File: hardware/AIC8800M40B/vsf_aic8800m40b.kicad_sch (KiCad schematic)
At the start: 102 parts, among them J1 USB_A, J2 USB_C_Receptacle_USB2.0, J3 USB_C_Receptacle_USB2.0, J4 Micro_SD_Card_Det1, J6 Conn_Coaxial, J7 Conn_Coaxial, J8 Conn_01x05, Q1 S9013, SW1 SW_Push, SW2 SW_Push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

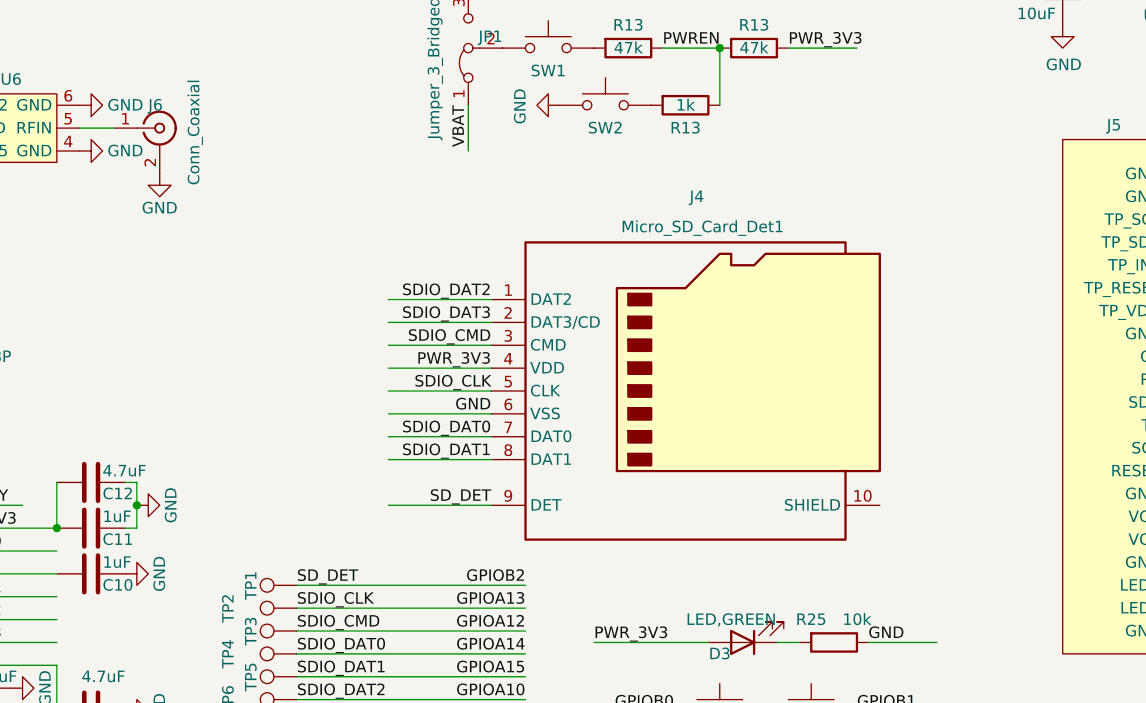
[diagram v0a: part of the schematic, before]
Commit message: [hardware/aic8800m40b] update to add 2.54 ext port
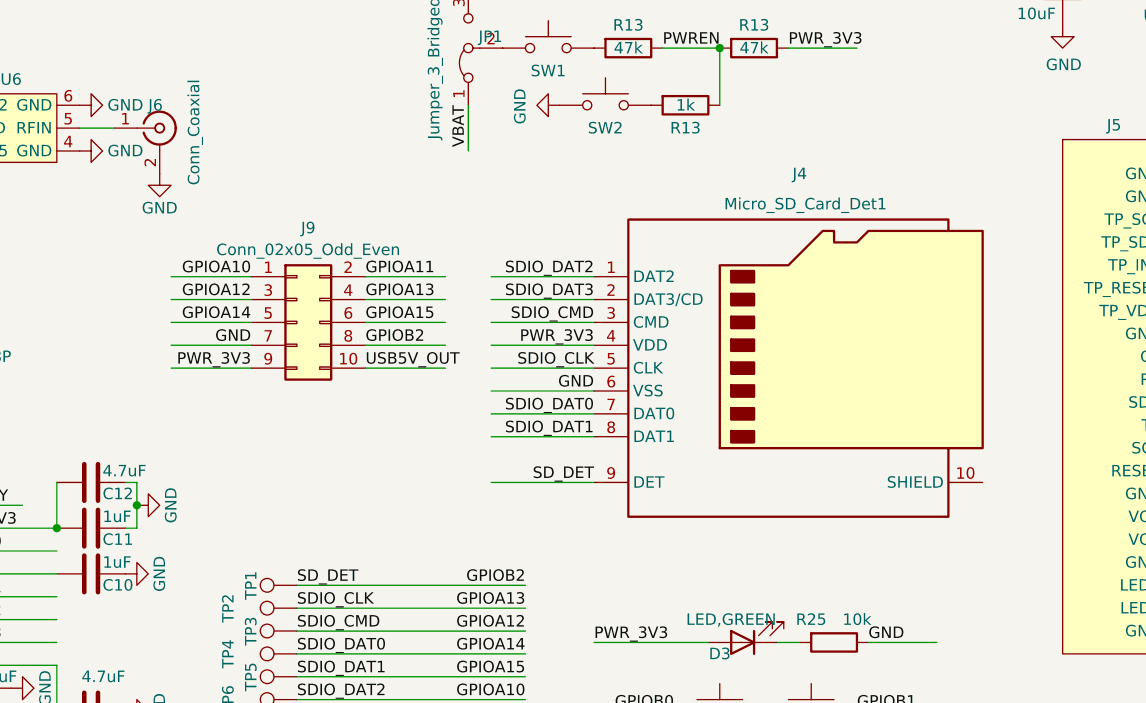
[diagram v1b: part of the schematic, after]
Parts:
- added J9: Conn_02x05_Odd_Even, Connector_PinHeader_2.54mm:PinHeader_2x05_P2.54mm_Horizontal, symbol Connector_Generic:Conn_02x05_Odd_Even
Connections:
- net GND: now also J9.7 (Pin_7)
- net GPIOA10: now also J9.1 (Pin_1)
- net GPIOA11: now also J9.2 (Pin_2)
- net GPIOA12: now also J9.3 (Pin_3)
- net GPIOA13: now also J9.4 (Pin_4)
- net GPIOA14: now also J9.5 (Pin_5)
- net GPIOA15: now also J9.6 (Pin_6)
- net GPIOB2: now also J9.8 (Pin_8)
- net PWR_3V3: now also J9.9 (Pin_9)
- net USB5V_OUT: now also J9.10 (Pin_10)
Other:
- moved on the sheet: J4

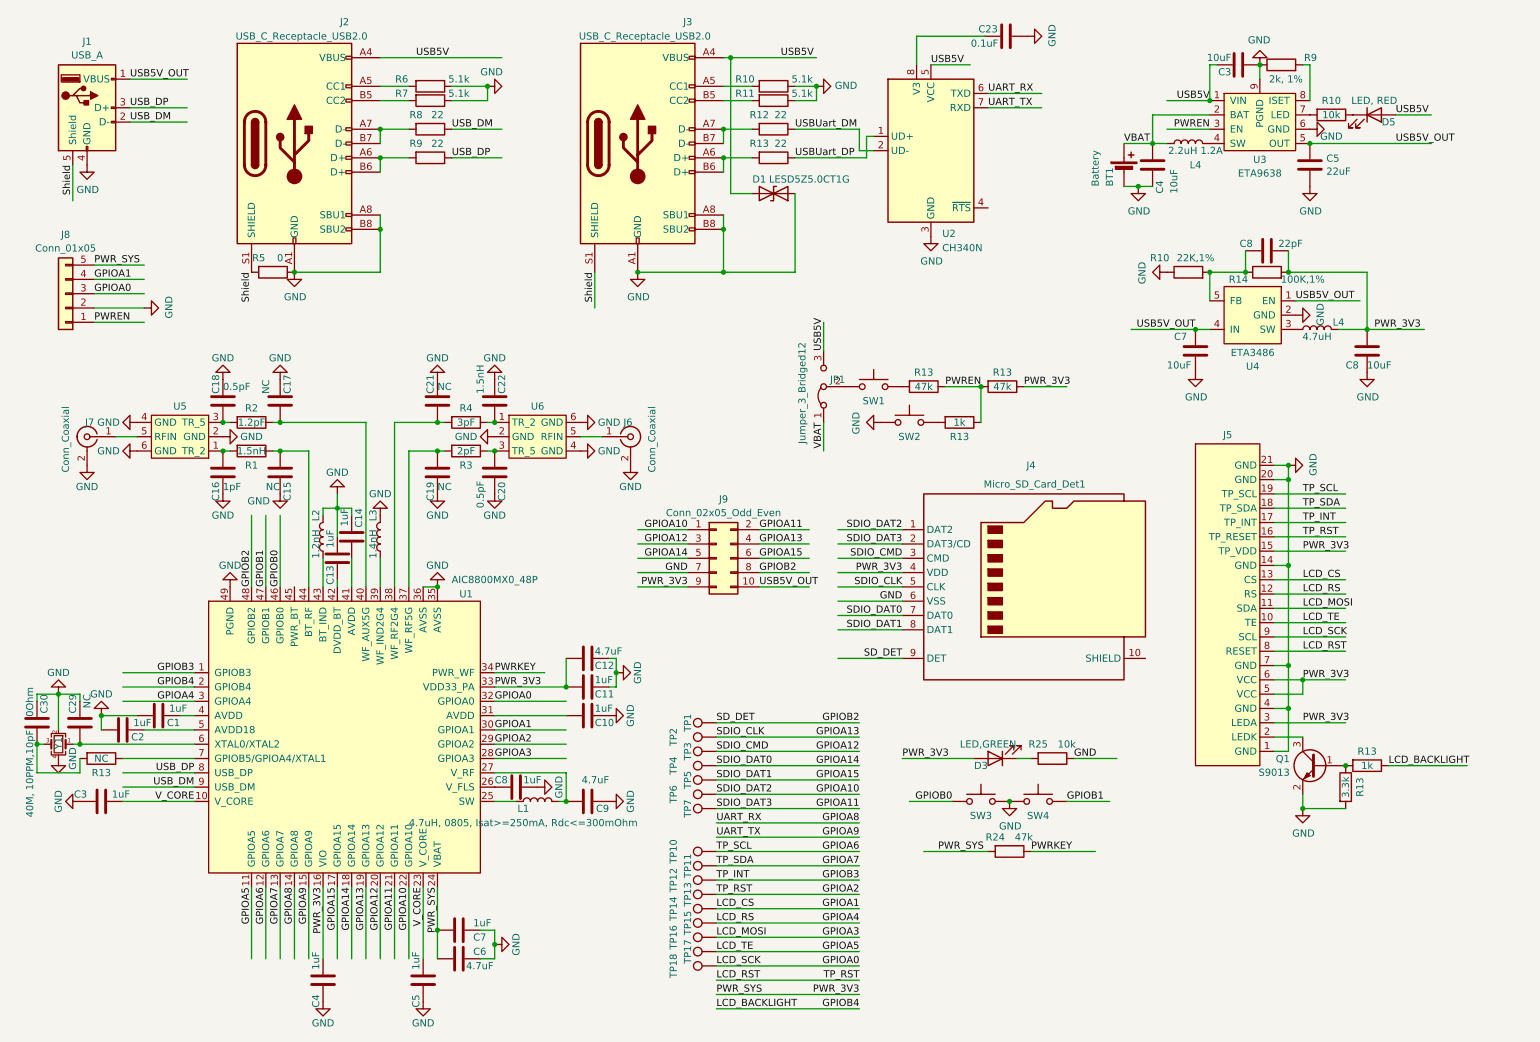
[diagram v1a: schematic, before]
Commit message: [hardware/aic8800m40b] add connector for all GPIOs
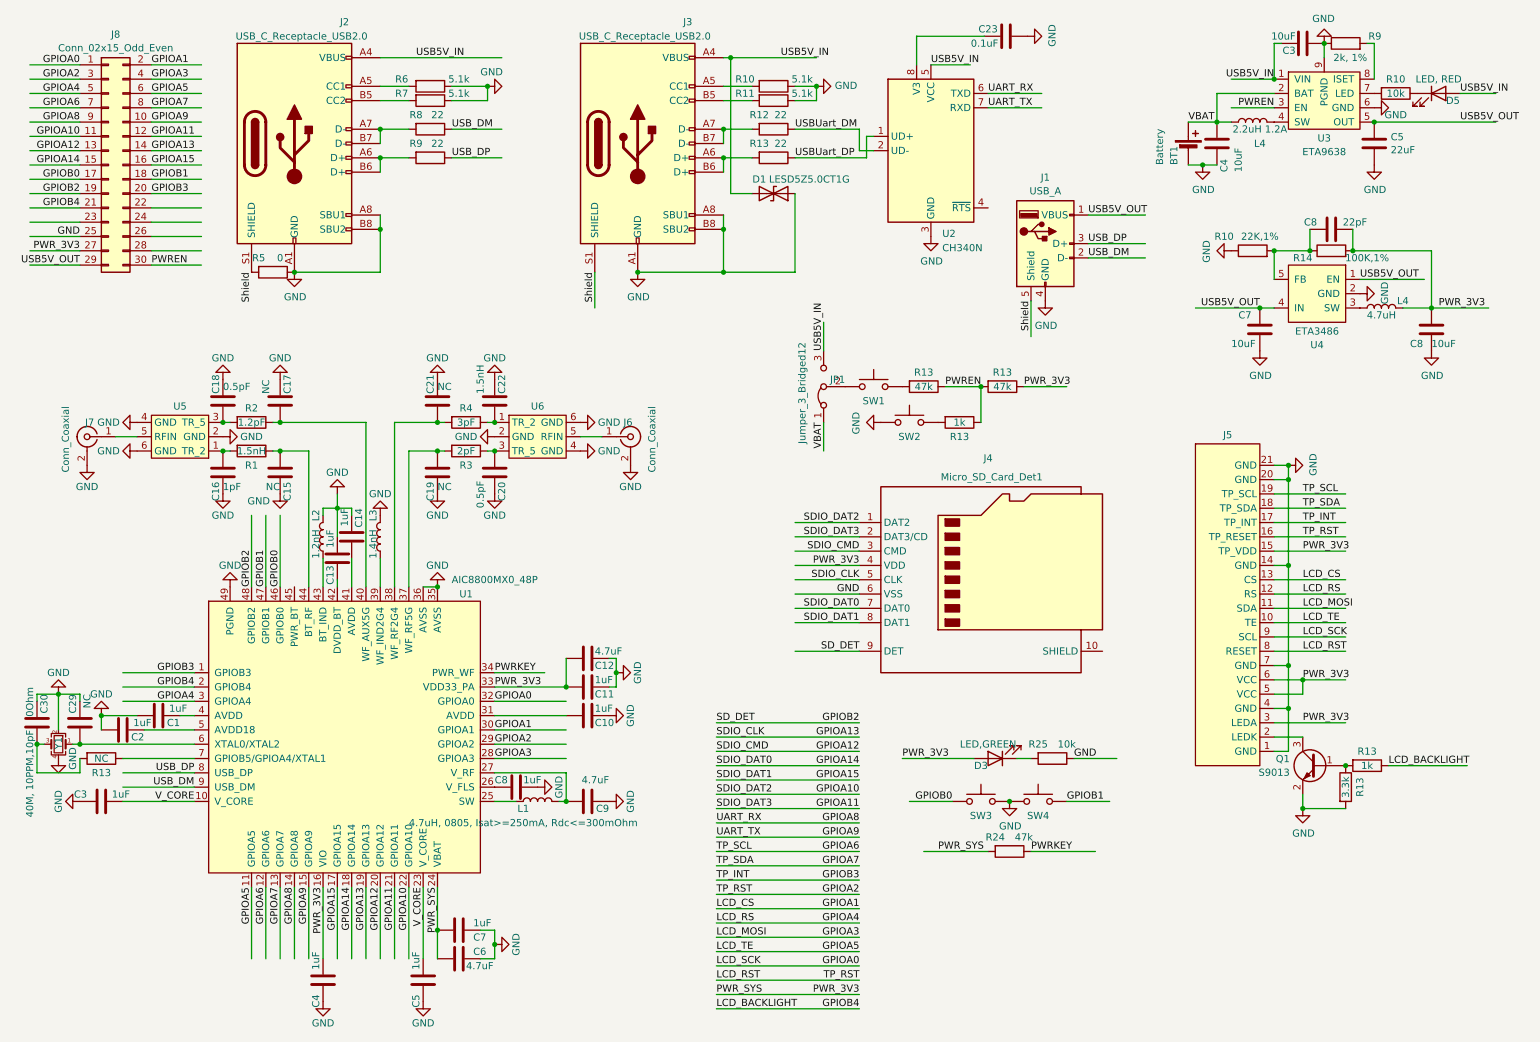
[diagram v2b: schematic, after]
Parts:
- removed J8: Conn_01x05, Connector_Harwin:Harwin_M20-89005xx_1x05_P2.54mm_Horizontal, symbol Connector_Generic:Conn_01x05
- removed J9: Conn_02x05_Odd_Even, Connector_PinHeader_2.54mm:PinHeader_2x05_P2.54mm_Horizontal, symbol Connector_Generic:Conn_02x05_Odd_Even
- removed TP1, TP10, TP11, TP12, TP13, TP14, TP15, TP16, TP17, TP18, TP2, TP3, TP4, TP5, TP6, TP7: TestPoint, TestPoint:TestPoint_Pad_D1.0mm, symbol Connector:TestPoint
- added J8: Conn_02x15_Odd_Even, Connector_PinHeader_2.54mm:PinHeader_2x15_P2.54mm_Horizontal, symbol Connector_Generic:Conn_02x15_Odd_Even
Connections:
- net GND: now also J8.25 (Pin_25)
- net GPIOA0: now also J8.1 (Pin_1)
- net GPIOA1: now also J8.2 (Pin_2)
- net GPIOA10: now also J8.11 (Pin_11)
- net GPIOA11: now also J8.12 (Pin_12)
- net GPIOA12: now also J8.13 (Pin_13)
- net GPIOA13: now also J8.14 (Pin_14)
- net GPIOA14: now also J8.15 (Pin_15)
- net GPIOA15: now also J8.16 (Pin_16)
- net GPIOA2: now also J8.3 (Pin_3)
- net GPIOA3: now also J8.4 (Pin_4)
- net GPIOA4: now also J8.5 (Pin_5)
- net GPIOA5: now also J8.6 (Pin_6)
- net GPIOA6: now also J8.7 (Pin_7)
- net GPIOA7: now also J8.8 (Pin_8)
- net GPIOA8: now also J8.9 (Pin_9)
- net GPIOA9: now also J8.10 (Pin_10)
- net GPIOB0: now also J8.17 (Pin_17)
- net GPIOB1: now also J8.18 (Pin_18)
- net GPIOB2: now also J8.19 (Pin_19)
- net GPIOB3: now also J8.20 (Pin_20)
- net GPIOB4: now also J8.21 (Pin_21)
- net PWREN: now also J8.30 (Pin_30)
- net PWR_3V3: now also J8.27 (Pin_27)
- net USB5V_OUT: now also J8.29 (Pin_29)
- net USB5V renamed USB5V_IN
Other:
- moved on the sheet: BT1, C3, C4, C5, C7, C8, D5, J1, J4, L4, R10, R14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

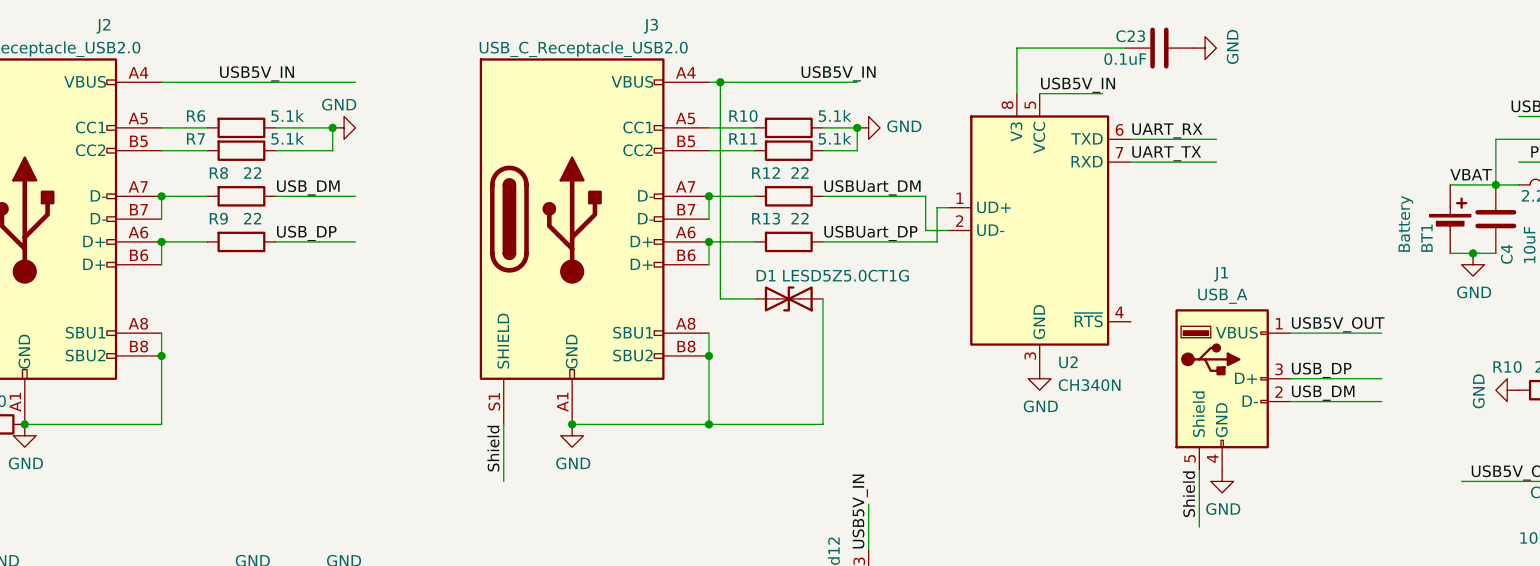
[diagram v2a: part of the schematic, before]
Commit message: [hardware/aic8800m40b] fix USB-A signals
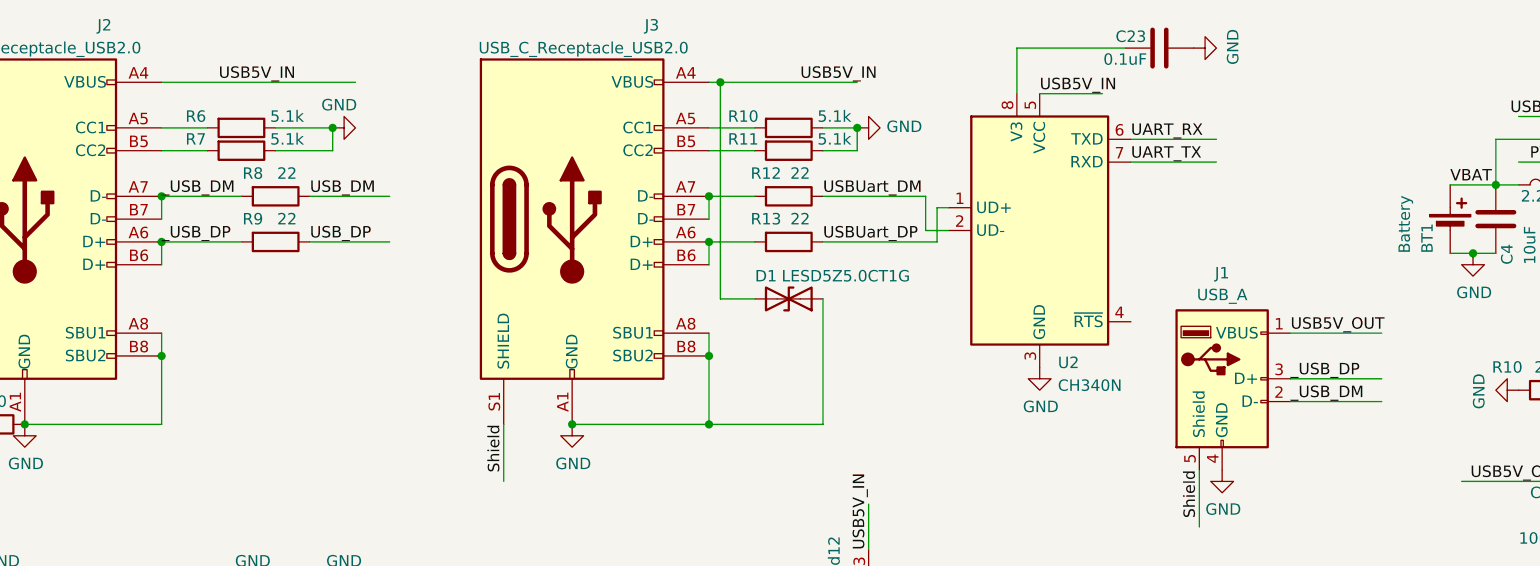
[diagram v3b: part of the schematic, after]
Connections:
- net USB_DM: no longer J1.2 (D-)
- net USB_DP: no longer J1.3 (D+)
- net _USB_DP: now reaches J2.A6 (D+), J2.B6 (D+), R9.2
- net _USB_DP: now also J1.3 (D+)
- net _USB_DM: now reaches J2.A7 (D-), J2.B7 (D-), R8.2
- net _USB_DM: now also J1.2 (D-)
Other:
- moved on the sheet: R8, R9
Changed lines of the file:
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@@
     (stroke (width 0) (type default))
   )
-  (wire (pts (xy 80.01 39.37) (xy 85.09 39.37))
+  (wire (pts (xy 80.01 39.37) (xy 88.9 39.37))
     (stroke (width 0) (type default))
   )
@@
     (stroke (width 0) (type default))
   )
-  (wire (pts (xy 92.71 34.29) (xy 101.6 34.29))
+  (wire (pts (xy 96.52 34.29) (xy 105.41 34.29))
     (stroke (width 0) (type default))
   )
@@
     (stroke (width 0) (type default))
   )
-  (wire (pts (xy 80.01 34.29) (xy 85.09 34.29))
+  (wire (pts (xy 80.01 34.29) (xy 88.9 34.29))
     (stroke (width 0) (type default))
   )
@@
     (stroke (width 0) (type default))
   )
-  (wire (pts (xy 92.71 39.37) (xy 101.6 39.37))
+  (wire (pts (xy 96.52 39.37) (xy 105.41 39.37))
     (stroke (width 0) (type default))
   )
@@
     (effects (font (size 1.27 1.27)) (justify right bottom))
   )
-  (label "USB_DP" (at 92.71 39.37 0) (fields_autoplaced)
+  (label "USB_DP" (at 96.52 39.37 0) (fields_autoplaced)
     (effects (font (size 1.27 1.27)) (justify left bottom))
   )
-  (label "USB_DP" (at 205.74 54.61 0) (fields_autoplaced)
+  (label "_USB_DP" (at 205.74 54.61 0) (fields_autoplaced)
     (effects (font (size 1.27 1.27)) (justify left bottom))
   )
@@
     (effects (font (size 1.27 1.27)) (justify right bottom))
   )
+  (label "_USB_DP" (at 80.01 39.37 0) (fields_autoplaced)
+    (effects (font (size 1.27 1.27)) (justify left bottom))
+  )
   (label "PWR_SYS" (at 139.7 187.96 0) (fields_autoplaced)
     (effects (font (size 1.27 1.27)) (justify left bottom))
@@
     (effects (font (size 1.27 1.27)) (justify right bottom))
   )
+  (label "_USB_DM" (at 80.01 34.29 0) (fields_autoplaced)
+    (effects (font (size 1.27 1.27)) (justify left bottom))
+  )
   (label "GPIOA6" (at 26.67 30.48 180) (fields_autoplaced)
     (effects (font (size 1.27 1.27)) (justify right bottom))
@@
     (effects (font (size 1.27 1.27)) (justify right bottom))
   )
-  (label "USB_DM" (at 205.74 57.15 0) (fields_autoplaced)
+  (label "_USB_DM" (at 205.74 57.15 0) (fields_autoplaced)
     (effects (font (size 1.27 1.27)) (justify left bottom))
   )
@@
     (effects (font (size 1.27 1.27)) (justify left bottom))
   )
-  (label "USB_DM" (at 92.71 34.29 0) (fields_autoplaced)
+  (label "USB_DM" (at 96.52 34.29 0) (fields_autoplaced)
     (effects (font (size 1.27 1.27)) (justify left bottom))
   )
@@
     )
   )
-  (symbol (lib_id "Device:R") (at 88.9 34.29 270) (unit 1)
+  (symbol (lib_id "Device:R") (at 92.71 34.29 270) (unit 1)
     (in_bom yes) (on_board yes) (dnp no)
-    (property "Reference" "R8" (at 86.36 31.75 90)
+    (property "Reference" "R8" (at 90.17 31.75 90)
       (effects (font (size 1.27 1.27)))
     )
-    (property "Value" "22" (at 90.17 31.75 90)
+    (property "Value" "22" (at 93.98 31.75 90)
       (effects (font (size 1.27 1.27)))
     )
-    (property "Footprint" "Resistor_SMD:R_0402_1005Metric" (at 88.9 32.512 90)
+    (property "Footprint" "Resistor_SMD:R_0402_1005Metric" (at 92.71 32.512 90)
       (effects (font (size 1.27 1.27)) hide)
     )
-    (property "Datasheet" "~" (at 88.9 34.29 0)
+    (property "Datasheet" "~" (at 92.71 34.29 0)
       (effects (font (size 1.27 1.27)) hide)
     )
@@
     )
   )
-  (symbol (lib_id "Device:R") (at 88.9 39.37 270) (unit 1)
+  (symbol (lib_id "Device:R") (at 92.71 39.37 270) (unit 1)
     (in_bom yes) (on_board yes) (dnp no)
-    (property "Reference" "R9" (at 86.36 36.83 90)
+    (property "Reference" "R9" (at 90.17 36.83 90)
       (effects (font (size 1.27 1.27)))
     )
-    (property "Value" "22" (at 90.17 36.83 90)
+    (property "Value" "22" (at 93.98 36.83 90)
       (effects (font (size 1.27 1.27)))
     )
-    (property "Footprint" "Resistor_SMD:R_0402_1005Metric" (at 88.9 37.592 90)
+    (property "Footprint" "Resistor_SMD:R_0402_1005Metric" (at 92.71 37.592 90)
       (effects (font (size 1.27 1.27)) hide)
     )
-    (property "Datasheet" "~" (at 88.9 39.37 0)
+    (property "Datasheet" "~" (at 92.71 39.37 0)
       (effects (font (size 1.27 1.27)) hide)
     )

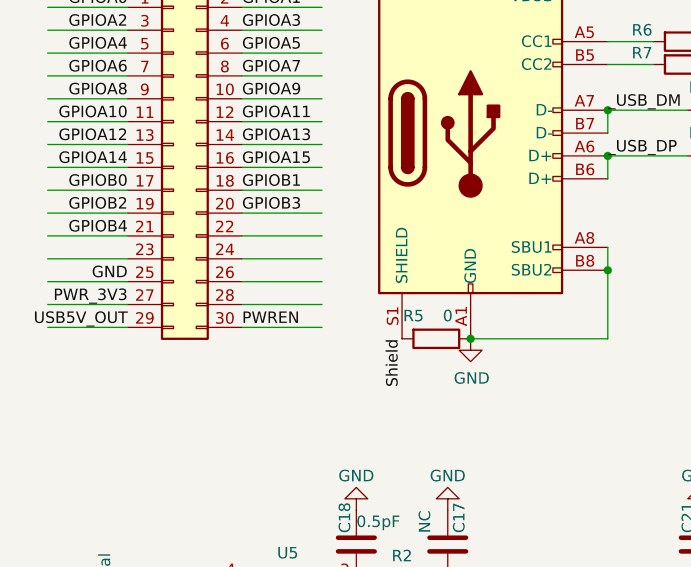
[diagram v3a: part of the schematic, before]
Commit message: [hardware/aic8800m40b] connect usb signals to pin header
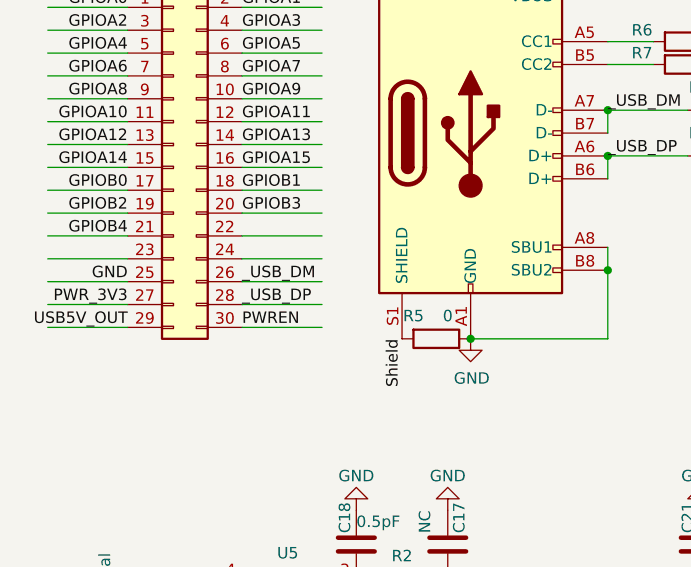
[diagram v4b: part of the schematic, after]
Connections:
- net _USB_DM: now also J8.26 (Pin_26)
- net _USB_DP: now also J8.28 (Pin_28)
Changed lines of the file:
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@@
+    (effects (font (size 1.27 1.27)) (justify left bottom))
+  )
+  (label "_USB_DP" (at 39.37 55.88 0) (fields_autoplaced)
     (effects (font (size 1.27 1.27)) (justify left bottom))
   )
@@
     (effects (font (size 1.27 1.27)) (justify left bottom))
   )
+  (label "_USB_DM" (at 39.37 53.34 0) (fields_autoplaced)
+    (effects (font (size 1.27 1.27)) (justify left bottom))
+  )
